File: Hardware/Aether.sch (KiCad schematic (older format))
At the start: 0 parts

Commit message: Radio schematic and rough layout
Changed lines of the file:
@@
 $Descr A4 11693 8268
 encoding utf-8
-Sheet 1 2
+Sheet 1 3
 Title "Aether - Pico Tracker"
 Date "17 aug 2014"
@@
 F5 "GPS_EN" I R 5600 3100 60
 $EndSheet
+$Sheet
+S 6600 3000 1000 1000
+U 53F09D80
+F0 "Radio" 60
+F1 "Radio.sch" 60
+F2 "LO_EN" I L 6600 3800 60
+F3 "LO_MOD" I L 6600 3900 60
+F4 "XCVR_SDN" I L 6600 3100 60
+F5 "~XCVR_INT" O L 6600 3600 60
+F6 "XCVR_SCLK" I L 6600 3200 60
+F7 "XCVR_MISO" O L 6600 3400 60
+F8 "XCVR_MOSI" I L 6600 3300 60
+F9 "~XCVR_SEL" I L 6600 3500 60
+F10 "TX" O R 7600 3100 60
+F11 "RAMP" O R 7600 3200 60
+F12 "RX" I R 7600 3300 60
+F13 "TX_SW" O R 7600 3500 60
+F14 "RX_SW" O R 7600 3600 60
+$EndSheet
 $EndSCHEMATC

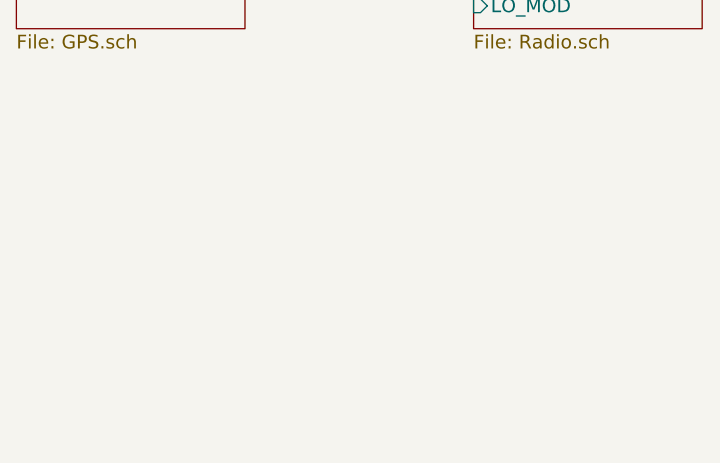
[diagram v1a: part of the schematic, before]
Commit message: 5v regulator schematic and rough layout
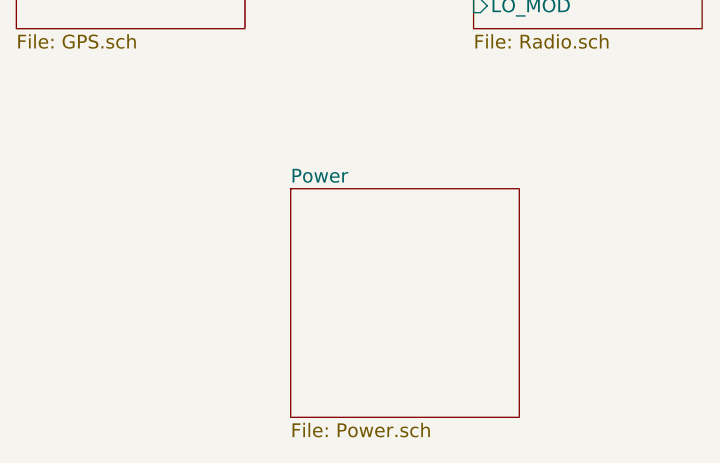
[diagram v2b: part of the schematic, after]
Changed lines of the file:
@@
 $Descr A4 11693 8268
 encoding utf-8
-Sheet 1 3
+Sheet 1 4
 Title "Aether - Pico Tracker"
-Date "17 aug 2014"
+Date "18 aug 2014"
 Rev "1"
 Comp "Aerodyne Labs"
@@
 F14 "RX_SW" O R 7600 3600 60
 $EndSheet
+$Sheet
+S 5800 4700 1000 1000
+U 53F1594C
+F0 "Power" 60
+F1 "Power.sch" 60
+$EndSheet
 $EndSCHEMATC

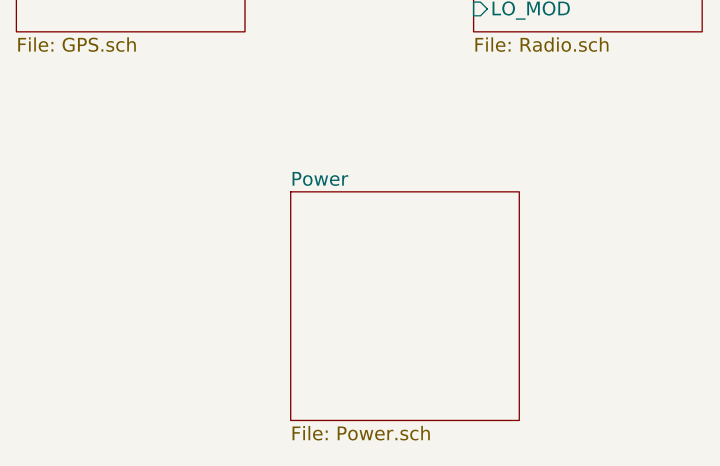
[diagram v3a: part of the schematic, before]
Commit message: Add charger and batteries to schematic and board
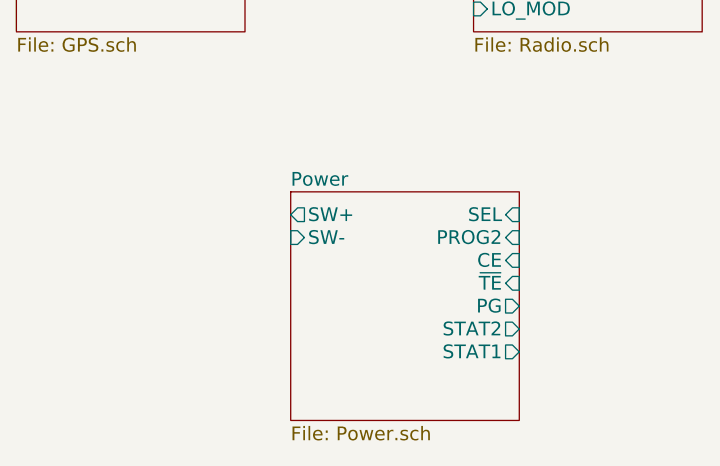
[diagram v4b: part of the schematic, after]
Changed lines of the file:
@@
 Sheet 1 4
 Title "Aether - Pico Tracker"
-Date "19 aug 2014"
+Date "29 aug 2014"
 Rev "1"
 Comp "Aerodyne Labs"
@@
 F0 "Power" 60
 F1 "Power.sch" 60
+F2 "SW+" O L 5800 4800 60
+F3 "SW-" I L 5800 4900 60
+F4 "SEL" I R 6800 4800 60
+F5 "PROG2" I R 6800 4900 60
+F6 "~TE" I R 6800 5100 60
+F7 "CE" I R 6800 5000 60
+F8 "PG" O R 6800 5200 60
+F9 "STAT2" O R 6800 5300 60
+F10 "STAT1" O R 6800 5400 60
 $EndSheet
 $EndSCHEMATC

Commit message: Core support circuitry
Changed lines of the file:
@@
 $Descr A4 11693 8268
 encoding utf-8
-Sheet 1 4
+Sheet 1 5
 Title "Aether - Pico Tracker"
-Date "29 aug 2014"
+Date "30 aug 2014"
 Rev "1"
 Comp "Aerodyne Labs"
@@
 $EndDescr
 $Sheet
-S 4600 3000 1000 1000
+S 3600 3000 1000 1000
 U 53F08CF1
 F0 "GPS" 60
 F1 "GPS.sch" 60
-F2 "GPS_PPS" O R 5600 3400 60
-F3 "GPS_MOSI" I R 5600 3200 60
-F4 "GPS_MISO" O R 5600 3300 60
-F5 "GPS_EN" I R 5600 3100 60
+F2 "GPS_PPS" O R 4600 3400 60
+F3 "GPS_MOSI" I R 4600 3200 60
+F4 "GPS_MISO" O R 4600 3300 60
+F5 "GPS_EN" I R 4600 3100 60
 $EndSheet
 $Sheet
-S 6600 3000 1000 1000
+S 7600 3000 1000 1000
 U 53F09D80
 F0 "Radio" 60
 F1 "Radio.sch" 60
-F2 "LO_EN" I L 6600 3800 60
-F3 "LO_MOD" I L 6600 3900 60
-F4 "XCVR_SDN" I L 6600 3100 60
-F5 "~XCVR_INT" O L 6600 3600 60
-F6 "XCVR_SCLK" I L 6600 3200 60
-F7 "XCVR_MISO" O L 6600 3400 60
-F8 "XCVR_MOSI" I L 6600 3300 60
-F9 "~XCVR_SEL" I L 6600 3500 60
-F10 "TX" O R 7600 3100 60
-F11 "RAMP" O R 7600 3200 60
-F12 "RX" I R 7600 3300 60
-F13 "TX_SW" O R 7600 3500 60
-F14 "RX_SW" O R 7600 3600 60
+F2 "LO_EN" I L 7600 3800 60
+F3 "LO_MOD" I L 7600 3900 60
+F4 "XCVR_SDN" I L 7600 3100 60
+F5 "~XCVR_INT" O L 7600 3600 60
+F6 "XCVR_SCLK" I L 7600 3200 60
+F7 "XCVR_MISO" O L 7600 3400 60
+F8 "XCVR_MOSI" I L 7600 3300 60
+F9 "~XCVR_SEL" I L 7600 3500 60
+F10 "TX" O R 8600 3100 60
+F11 "RAMP" O R 8600 3200 60
+F12 "RX" I R 8600 3300 60
+F13 "TX_SW" O R 8600 3500 60
+F14 "RX_SW" O R 8600 3600 60
 $EndSheet
 $Sheet
-S 5800 4700 1000 1000
+S 5600 5000 1000 1000
 U 53F1594C
 F0 "Power" 60
 F1 "Power.sch" 60
-F2 "SW+" O L 5800 4800 60
-F3 "SW-" I L 5800 4900 60
-F4 "SEL" I R 6800 4800 60
-F5 "PROG2" I R 6800 4900 60
-F6 "~TE" I R 6800 5100 60
-F7 "CE" I R 6800 5000 60
-F8 "PG" O R 6800 5200 60
-F9 "STAT2" O R 6800 5300 60
-F10 "STAT1" O R 6800 5400 60
+F2 "SW+" O L 5600 5100 60
+F3 "SW-" I L 5600 5200 60
+F4 "SEL" I R 6600 5100 60
+F5 "PROG2" I R 6600 5200 60
+F6 "~TE" I R 6600 5400 60
+F7 "CE" I R 6600 5300 60
+F8 "PG" O R 6600 5500 60
+F9 "STAT2" O R 6600 5600 60
+F10 "STAT1" O R 6600 5700 60
+$EndSheet
+$Sheet
+S 5600 3000 1000 1000
+U 5400F413
+F0 "Core" 60
+F1 "Core.sch" 60
+F2 "USB_DM" B R 6600 3200 60
+F3 "USB_DP" B R 6600 3100 60
 $EndSheet
 $EndSCHEMATC

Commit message: Add usb
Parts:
- added J2: USB_MINI, ~, symbol USB_MINI
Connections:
- net labels added: +5VP, GND
- wire segments 0 -> 17
- no-connect marks 0 -> 1
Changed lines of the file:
@@
 $EndSheet
 $Sheet
-S 7600 3000 1000 1000
+S 7600 3300 1000 1000
 U 53F09D80
 F0 "Radio" 60
 F1 "Radio.sch" 60
-F2 "LO_EN" I L 7600 3800 60
-F3 "LO_MOD" I L 7600 3900 60
-F4 "XCVR_SDN" I L 7600 3100 60
-F5 "~XCVR_INT" O L 7600 3600 60
-F6 "XCVR_SCLK" I L 7600 3200 60
-F7 "XCVR_MISO" O L 7600 3400 60
-F8 "XCVR_MOSI" I L 7600 3300 60
-F9 "~XCVR_SEL" I L 7600 3500 60
-F10 "TX" O R 8600 3100 60
-F11 "RAMP" O R 8600 3200 60
-F12 "RX" I R 8600 3300 60
-F13 "TX_SW" O R 8600 3500 60
-F14 "RX_SW" O R 8600 3600 60
+F2 "LO_EN" I L 7600 4100 60
+F3 "LO_MOD" I L 7600 4200 60
+F4 "XCVR_SDN" I L 7600 3400 60
+F5 "~XCVR_INT" O L 7600 3900 60
+F6 "XCVR_SCLK" I L 7600 3500 60
+F7 "XCVR_MISO" O L 7600 3700 60
+F8 "XCVR_MOSI" I L 7600 3600 60
+F9 "~XCVR_SEL" I L 7600 3800 60
+F10 "TX" O R 8600 3400 60
+F11 "RAMP" O R 8600 3500 60
+F12 "RX" I R 8600 3600 60
+F13 "TX_SW" O R 8600 3800 60
+F14 "RX_SW" O R 8600 3900 60
 $EndSheet
 $Sheet
@@
 F0 "Core" 60
 F1 "Core.sch" 60
-F2 "USB_DM" B R 6600 3200 60
-F3 "USB_DP" B R 6600 3100 60
+F2 "USB_DM" B R 6600 3100 60
+F3 "USB_DP" B R 6600 3200 60
+F4 "XCVR_MOSI" O R 6600 3600 60
+F5 "XCVR_MISO" I R 6600 3700 60
+F6 "XCVR_SCLK" O R 6600 3500 60
+F7 "~XCVR_SEL" O R 6600 3800 60
+F8 "~XCVR_INT" I R 6600 3900 60
+F9 "XCVR_SDN" O R 6600 3400 60
 $EndSheet
+Wire Wire Line
+	6600 3400 7600 3400
+Wire Wire Line
+	6600 3500 7600 3500
+Wire Wire Line
+	6600 3600 7600 3600
+Wire Wire Line
+	6600 3700 7600 3700
+Wire Wire Line
+	6600 3800 7600 3800
+Wire Wire Line
+	6600 3900 7600 3900
+$Comp
+L USB_MINI J2
+U 1 1 5401342F
+P 8100 1950
+F 0 "J2" H 8100 2300 60  0000 C CNN
+F 1 "USB_MINI" H 8100 1600 50  0000 C CNN
+F 2 "~" H 8100 2000 60  0000 C CNN
+F 3 "~" H 8100 2000 60  0000 C CNN
+	1    8100 1950
+	1    0    0    -1
+$EndComp
+$Comp
+L GND #PWR01
+U 1 1 540135D6
+P 7700 2300
+F 0 "#PWR01" H 7700 2300 30  0001 C CNN
+F 1 "GND" H 7700 2230 30  0001 C CNN
+F 2 "" H 7700 2300 60  0000 C CNN
+F 3 "" H 7700 2300 60  0000 C CNN
+	1    7700 2300
+	1    0    0    -1
+$EndComp
+$Comp
+L +5VP #PWR02
+U 1 1 540135E5
+P 7700 1600
+F 0 "#PWR02" H 7700 1690 20  0001 C CNN
+F 1 "+5VP" H 7700 1690 30  0000 C CNN
+F 2 "" H 7700 1600 60  0000 C CNN
+F 3 "" H 7700 1600 60  0000 C CNN
+	1    7700 1600
+	1    0    0    -1
+$EndComp
+Wire Wire Line
+	7700 1600 7700 1700
+Wire Wire Line
+	7700 1700 7800 1700
+Wire Wire Line
+	7800 2100 7700 2100
+Wire Wire Line
+	7700 2100 7700 2300
+Wire Wire Line
+	7800 2200 7700 2200
+Connection ~ 7700 2200
+NoConn ~ 7800 2000
+Wire Wire Line
+	7800 1800 7100 1800
+Wire Wire Line
+	7100 1800 7100 3100
+Wire Wire Line
+	7100 3100 6600 3100
+Wire Wire Line
+	6600 3200 7200 3200
+Wire Wire Line
+	7200 3200 7200 1900
+Wire Wire Line
+	7200 1900 7800 1900
 $EndSCHEMATC

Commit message: Connect subsystems
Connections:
- wire segments 17 -> 23
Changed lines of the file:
@@
 $EndDescr
 $Sheet
-S 3600 3000 1000 1000
+S 3100 3000 1000 1000
 U 53F08CF1
 F0 "GPS" 60
 F1 "GPS.sch" 60
-F2 "GPS_PPS" O R 4600 3400 60
-F3 "GPS_MOSI" I R 4600 3200 60
-F4 "GPS_MISO" O R 4600 3300 60
-F5 "GPS_EN" I R 4600 3100 60
+F2 "GPS_PPS" O R 4100 3400 60
+F3 "GPS_MOSI" I R 4100 3200 60
+F4 "GPS_MISO" O R 4100 3300 60
+F5 "GPS_EN" I R 4100 3100 60
 $EndSheet
 $Sheet
@@
 F9 "STAT2" O R 6600 5600 60
 F10 "STAT1" O R 6600 5700 60
-$EndSheet
-$Sheet
-S 5600 3000 1000 1000
-U 5400F413
-F0 "Core" 60
-F1 "Core.sch" 60
-F2 "USB_DM" B R 6600 3100 60
-F3 "USB_DP" B R 6600 3200 60
-F4 "XCVR_MOSI" O R 6600 3600 60
-F5 "XCVR_MISO" I R 6600 3700 60
-F6 "XCVR_SCLK" O R 6600 3500 60
-F7 "~XCVR_SEL" O R 6600 3800 60
-F8 "~XCVR_INT" I R 6600 3900 60
-F9 "XCVR_SDN" O R 6600 3400 60
 $EndSheet
 Wire Wire Line
@@
 Wire Wire Line
 	7200 1900 7800 1900
+$Sheet
+S 5100 3000 1500 1300
+U 5400F413
+F0 "Core" 60
+F1 "Core.sch" 60
+F2 "USB_DM" B R 6600 3100 60
+F3 "USB_DP" B R 6600 3200 60
+F4 "XCVR_MOSI" O R 6600 3600 60
+F5 "XCVR_MISO" I R 6600 3700 60
+F6 "XCVR_SCLK" O R 6600 3500 60
+F7 "~XCVR_SEL" O R 6600 3800 60
+F8 "~XCVR_INT" I R 6600 3900 60
+F9 "XCVR_SDN" O R 6600 3400 60
+F10 "LO_EN" O R 6600 4100 60
+F11 "LO_MOD" O R 6600 4200 60
+F12 "GPS_MOSI" O L 5100 3200 60
+F13 "GPS_MISO" I L 5100 3300 60
+F14 "GPS_EN" O L 5100 3100 60
+F15 "GPS_PPS" I L 5100 3400 60
+$EndSheet
+Wire Wire Line
+	4100 3100 5100 3100
+Wire Wire Line
+	4100 3200 5100 3200
+Wire Wire Line
+	4100 3300 5100 3300
+Wire Wire Line
+	4100 3400 5100 3400
+Wire Wire Line
+	6600 4100 7600 4100
+Wire Wire Line
+	6600 4200 7600 4200
 $EndSCHEMATC

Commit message: Clear hardware for new version
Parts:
- removed J2: USB_MINI, ~, symbol USB_MINI
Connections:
- net labels removed: +5VP, GND
- wire segments 23 -> 0
- no-connect marks 1 -> 0
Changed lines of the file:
@@
 EESchema Schematic File Version 2
 LIBS:power
-LIBS:Aerodyne_v2
-LIBS:Aether-cache
-EELAYER 27 0
+LIBS:SiliconLabs
+LIBS:STMicroelectronics
+EELAYER 25 0
 EELAYER END
 $Descr A4 11693 8268
 encoding utf-8
-Sheet 1 5
+Sheet 1 1
 Title "Aether - Pico Tracker"
 Date "30 aug 2014"
@@
 Comment4 ""
 $EndDescr
-$Sheet
-S 3100 3000 1000 1000
-U 53F08CF1
-F0 "GPS" 60
-F1 "GPS.sch" 60
-F2 "GPS_PPS" O R 4100 3400 60
-F3 "GPS_MOSI" I R 4100 3200 60
-F4 "GPS_MISO" O R 4100 3300 60
-F5 "GPS_EN" I R 4100 3100 60
-$EndSheet
-$Sheet
-S 7600 3300 1000 1000
-U 53F09D80
-F0 "Radio" 60
-F1 "Radio.sch" 60
-F2 "LO_EN" I L 7600 4100 60
-F3 "LO_MOD" I L 7600 4200 60
-F4 "XCVR_SDN" I L 7600 3400 60
-F5 "~XCVR_INT" O L 7600 3900 60
-F6 "XCVR_SCLK" I L 7600 3500 60
-F7 "XCVR_MISO" O L 7600 3700 60
-F8 "XCVR_MOSI" I L 7600 3600 60
-F9 "~XCVR_SEL" I L 7600 3800 60
-F10 "TX" O R 8600 3400 60
-F11 "RAMP" O R 8600 3500 60
-F12 "RX" I R 8600 3600 60
-F13 "TX_SW" O R 8600 3800 60
-F14 "RX_SW" O R 8600 3900 60
-$EndSheet
-$Sheet
-S 5600 5000 1000 1000
-U 53F1594C
-F0 "Power" 60
-F1 "Power.sch" 60
-F2 "SW+" O L 5600 5100 60
-F3 "SW-" I L 5600 5200 60
-F4 "SEL" I R 6600 5100 60
-F5 "PROG2" I R 6600 5200 60
-F6 "~TE" I R 6600 5400 60
-F7 "CE" I R 6600 5300 60
-F8 "PG" O R 6600 5500 60
-F9 "STAT2" O R 6600 5600 60
-F10 "STAT1" O R 6600 5700 60
-$EndSheet
-Wire Wire Line
-	6600 3400 7600 3400
-Wire Wire Line
-	6600 3500 7600 3500
-Wire Wire Line
-	6600 3600 7600 3600
-Wire Wire Line
-	6600 3700 7600 3700
-Wire Wire Line
-	6600 3800 7600 3800
-Wire Wire Line
-	6600 3900 7600 3900
-$Comp
-L USB_MINI J2
-U 1 1 5401342F
-P 8100 1950
-F 0 "J2" H 8100 2300 60  0000 C CNN
-F 1 "USB_MINI" H 8100 1600 50  0000 C CNN
-F 2 "~" H 8100 2000 60  0000 C CNN
-F 3 "~" H 8100 2000 60  0000 C CNN
-	1    8100 1950
-	1    0    0    -1
-$EndComp
-$Comp
-L GND #PWR01
-U 1 1 540135D6
-P 7700 2300
-F 0 "#PWR01" H 7700 2300 30  0001 C CNN
-F 1 "GND" H 7700 2230 30  0001 C CNN
-F 2 "" H 7700 2300 60  0000 C CNN
-F 3 "" H 7700 2300 60  0000 C CNN
-	1    7700 2300
-	1    0    0    -1
-$EndComp
-$Comp
-L +5VP #PWR02
-U 1 1 540135E5
-P 7700 1600
-F 0 "#PWR02" H 7700 1690 20  0001 C CNN
-F 1 "+5VP" H 7700 1690 30  0000 C CNN
-F 2 "" H 7700 1600 60  0000 C CNN
-F 3 "" H 7700 1600 60  0000 C CNN
-	1    7700 1600
-	1    0    0    -1
-$EndComp
-Wire Wire Line
-	7700 1600 7700 1700
-Wire Wire Line
-	7700 1700 7800 1700
-Wire Wire Line
-	7800 2100 7700 2100
-Wire Wire Line
-	7700 2100 7700 2300
-Wire Wire Line
-	7800 2200 7700 2200
-Connection ~ 7700 2200
-NoConn ~ 7800 2000
-Wire Wire Line
-	7800 1800 7100 1800
-Wire Wire Line
-	7100 1800 7100 3100
-Wire Wire Line
-	7100 3100 6600 3100
-Wire Wire Line
-	6600 3200 7200 3200
-Wire Wire Line
-	7200 3200 7200 1900
-Wire Wire Line
-	7200 1900 7800 1900
-$Sheet
-S 5100 3000 1500 1300
-U 5400F413
-F0 "Core" 60
-F1 "Core.sch" 60
-F2 "USB_DM" B R 6600 3100 60
-F3 "USB_DP" B R 6600 3200 60
-F4 "XCVR_MOSI" O R 6600 3600 60
-F5 "XCVR_MISO" I R 6600 3700 60
-F6 "XCVR_SCLK" O R 6600 3500 60
-F7 "~XCVR_SEL" O R 6600 3800 60
-F8 "~XCVR_INT" I R 6600 3900 60
-F9 "XCVR_SDN" O R 6600 3400 60
-F10 "LO_EN" O R 6600 4100 60
-F11 "LO_MOD" O R 6600 4200 60
-F12 "GPS_MOSI" O L 5100 3200 60
-F13 "GPS_MISO" I L 5100 3300 60
-F14 "GPS_EN" O L 5100 3100 60
-F15 "GPS_PPS" I L 5100 3400 60
-$EndSheet
-Wire Wire Line
-	4100 3100 5100 3100
-Wire Wire Line
-	4100 3200 5100 3200
-Wire Wire Line
-	4100 3300 5100 3300
-Wire Wire Line
-	4100 3400 5100 3400
-Wire Wire Line
-	6600 4100 7600 4100
-Wire Wire Line
-	6600 4200 7600 4200
 $EndSCHEMATC
